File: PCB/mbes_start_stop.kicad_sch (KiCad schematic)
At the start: 13 parts, among them Q10 BC817, Q12 BC817, Q17 BC327, Q18 BC327, U4 HK19F-DC12-SHG

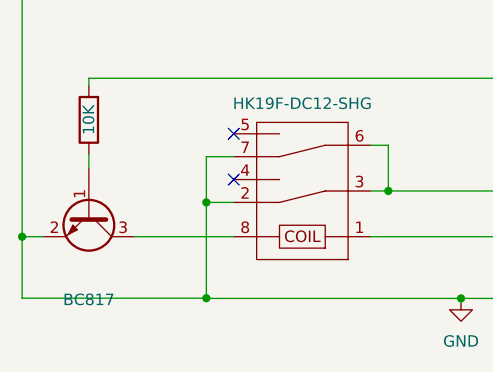
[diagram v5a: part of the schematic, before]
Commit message: Many changes
- The power drivers component has been implemented with TPCA8120 P-ch MOSfet
- The temp-power management has been moved from pcb-a to pcb-b
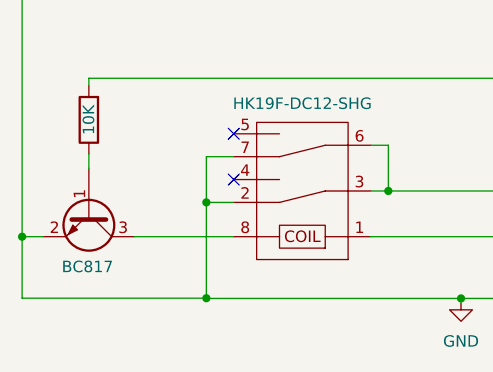
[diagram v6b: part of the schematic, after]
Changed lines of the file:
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@@
   )
   (symbol (lib_id "Transistor_BJT:BC817") (at 81.1784 145.5928 270) (unit 1)
-    (in_bom yes) (on_board yes) (dnp no) (fields_autoplaced)
+    (in_bom yes) (on_board yes) (dnp no)
     (property "Reference" "Q12" (at 81.1784 152.6032 90)
       (effects (font (size 1.27 1.27)) hide)
     )
-    (property "Value" "BC817" (at 81.1784 155.1432 90)
+    (property "Value" "BC817" (at 81.026 151.4856 90)
       (effects (font (size 1.27 1.27)))
     )

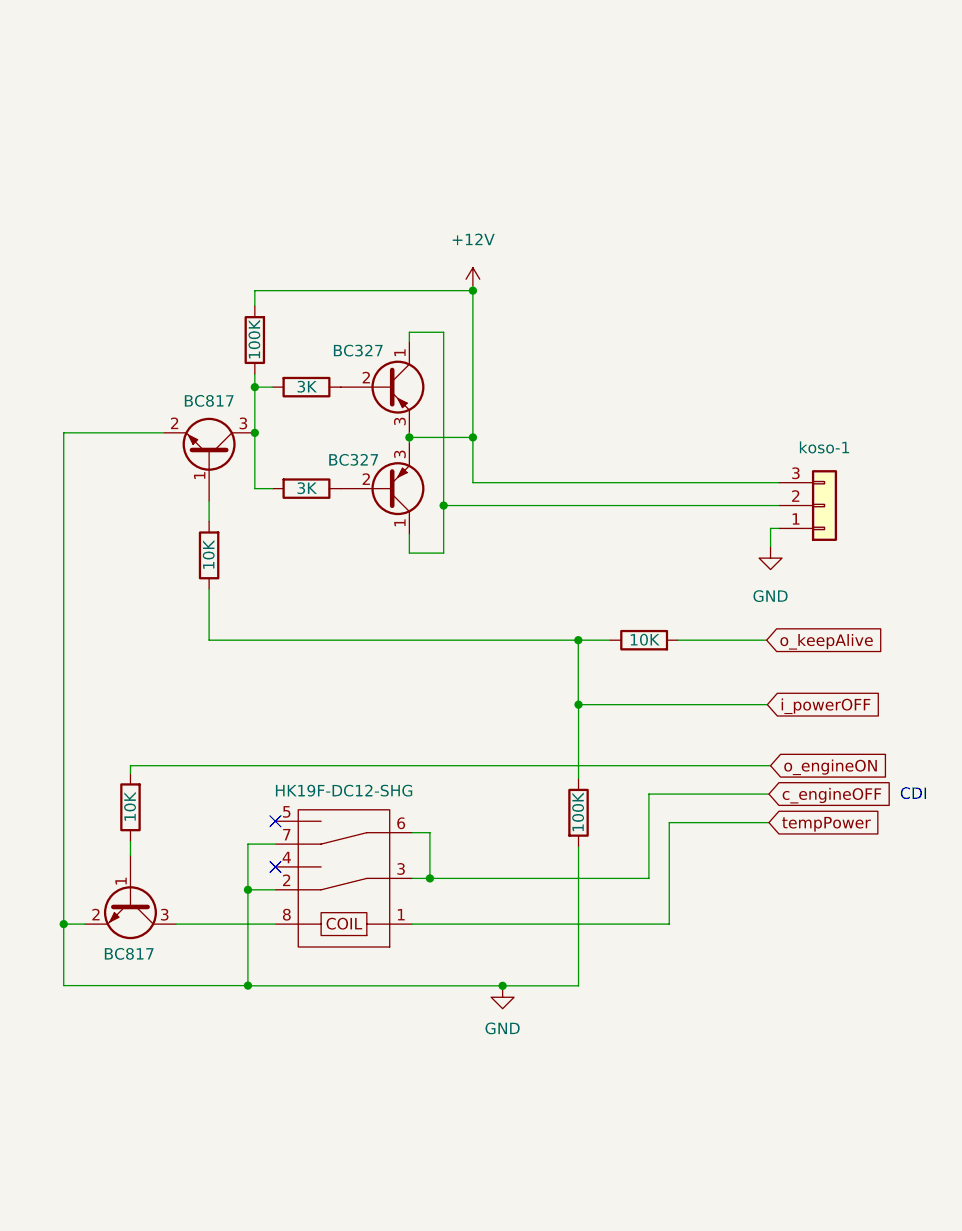
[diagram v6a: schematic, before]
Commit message: SSR replace mechanical retlay
Not yet been tested
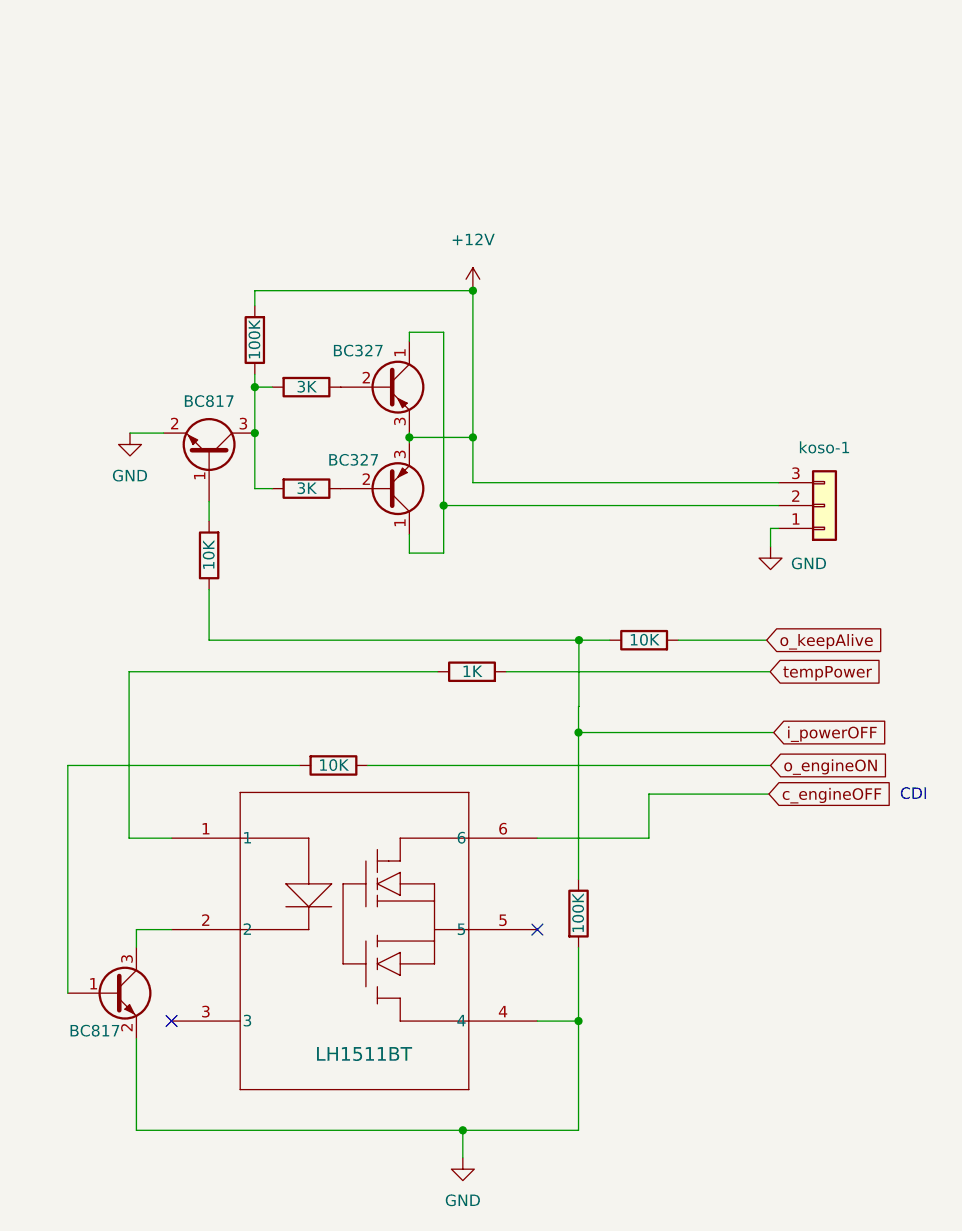
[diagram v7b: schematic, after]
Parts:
- removed U4: HK19F-DC12-SHG, HK19F:HK19F-DC12-SHG, symbol HK19F:HK19F-DC12-SHG
- added RA23: 1K, Resistor_SMD:R_1206_3216Metric, symbol Device:R
- added U5: LH1511BT, LH1511BT:DIP_1511BT_VIS, symbol LH1511BT:LH1511BT
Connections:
- net GND: now also U5.4
- net c_engineOFF: now also U5.6
- net o_engineON: now also RA44.1; no longer RA44.2
- net tempPower: now also RA23.2
- net at Q12.1 (B): now also RA44.2; no longer RA44.1
- net at Q12.3 (C): now also U5.2
- new net: RA23.1, U5.1

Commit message: Changes and enhancements
- File porting to Kicad-8
- SSR has been replaced by Mosfet deplation N-Channel
- "to-PCB-a-1" connector has been changed with tree pins one
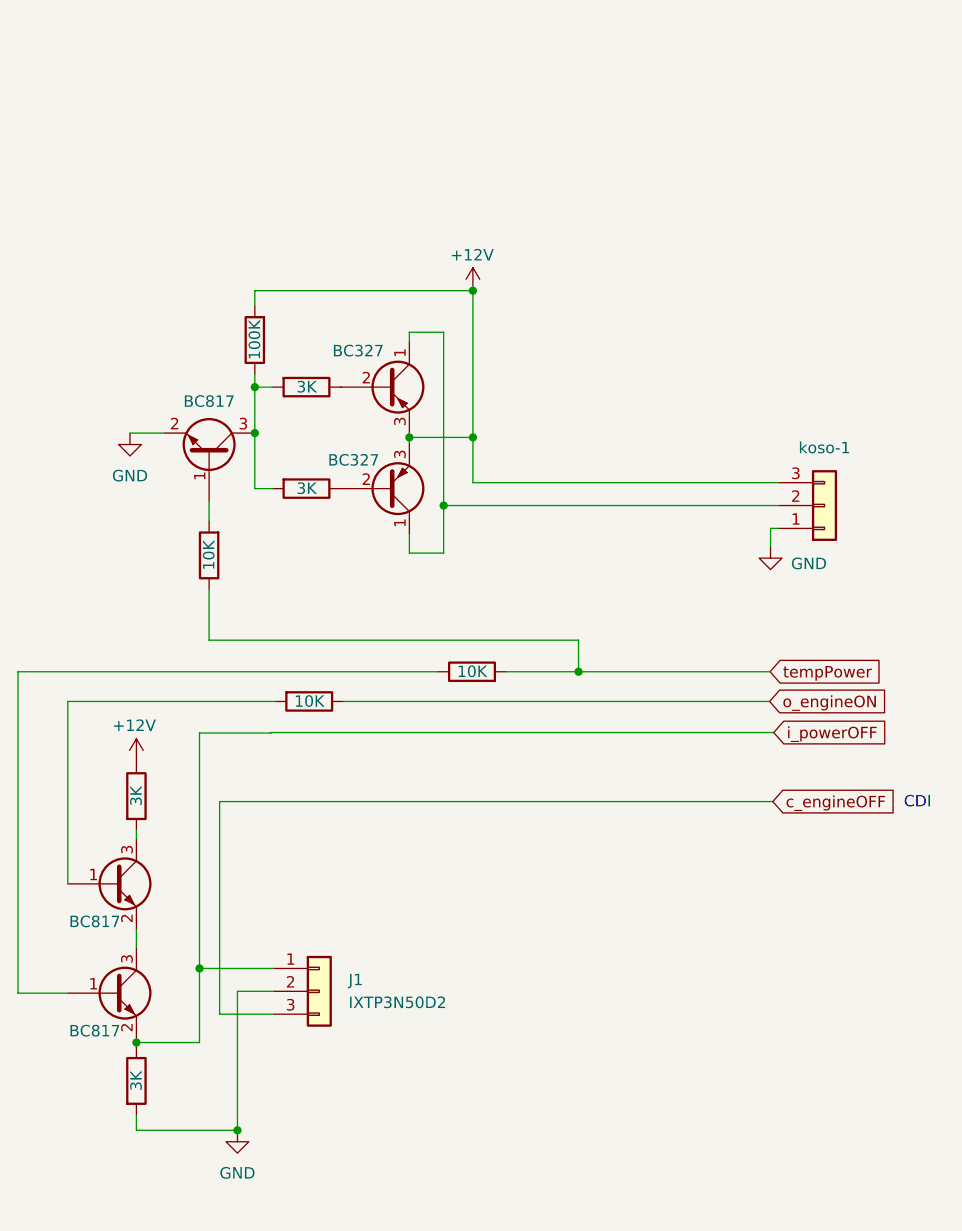
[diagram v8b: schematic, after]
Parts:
- removed RA41: 100K, Resistor_SMD:R_1206_3216Metric, symbol Device:R
- removed U5: LH1511BT, LH1511BT:DIP_1511BT_VIS, symbol LH1511BT:LH1511BT
- added J1: IXTP3N50D2, Connector_PinHeader_1.27mm:PinHeader_1x03_P1.27mm_Horizontal, symbol Connector_Generic:Conn_01x03
- added Q16: BC817, Package_TO_SOT_SMD:SOT-23, symbol Transistor_BJT:BC817
- added RA29: 3K, Resistor_SMD:R_1206_3216Metric, symbol Device:R
- RA23: value 1K -> 10K
- RA43: value 10K -> 3K
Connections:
- net +12V: now also RA43.1
- net GND: now also J1.2 (Pin_2), RA29.2; no longer Q12.2 (E)
- net c_engineOFF: now also J1.3 (Pin_3)
- net i_powerOFF: now also Q12.2 (E), J1.1 (Pin_1), RA29.1; no longer RA43.1, RA8.1
- net tempPower: now also RA8.1
- net at RA44.2: now also Q16.1 (B); no longer Q12.1 (B)
- net at Q12.3 (C): now also Q16.2 (E)
- net at RA23.1: now also Q12.1 (B)
- net o_keepAlive: no longer names the net of RA43.2
- net o_keepAlive: now also Q16.3 (C)
- no-connect marks 2 -> 0
